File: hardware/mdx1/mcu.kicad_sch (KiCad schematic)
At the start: 37 parts, among them J5 SWD 10p 1.27mm, J6 microSD (Hirose DM3AT), U22 STM32H743ZIT6, Y1 16.384 MHz 3225, Y2 32.768 kHz 3215

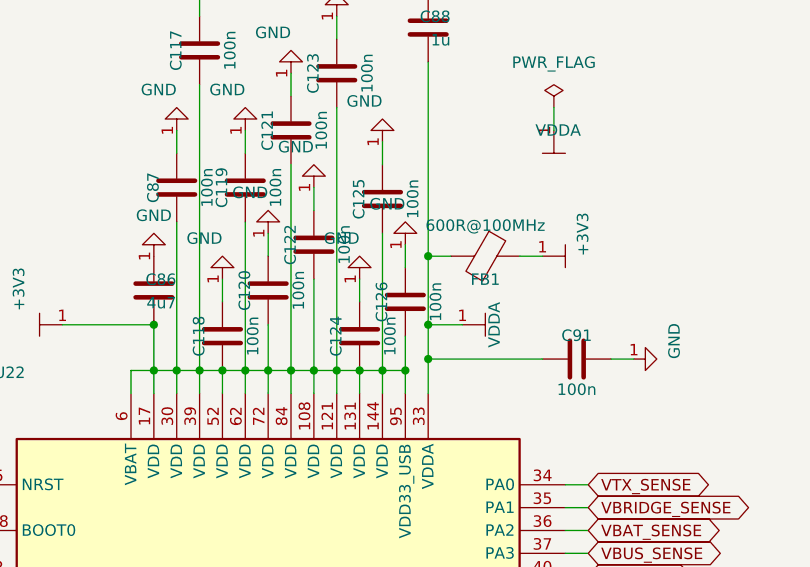
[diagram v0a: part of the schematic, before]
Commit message: Re-source out-of-stock parts; rework D8/9 footprint and GNSS antenna front end
Parts re-sourced to in-stock equivalents (BOM + board + firmware kept in sync):
- U4  TPS65131RGET, U12 INA241A2QDGKRQ1, U23 LSM6DSO32TR (same footprints)
- Q1  SiR680ADP-T1-UE3 (80 V, same PowerPAK SO-8; higher Qg - verify gate drive)
- U2  BQ27441DRZT-G1A (drop-in, R9 sense retained)
- D8/9 NSVBAT54SWT1G: SOT-323/SC-70 dual-series wired as a single diode
  (anode=pin1, cathode=pin3, pin2 NC); footprint changed on the board
- C32/C33/C38-48 re-sourced (KEMET/Murata/TDK), same footprints

GNSS antenna: chip antenna -> external active antenna via u.FL
- Removed U28 (chip antenna), C115 (match pad), R111 (0R RF series-match)
- Added J13 u.FL (Molex 73412-0110) + bias-tee: L8 27nH feed, C127 33pF DC block,
  C128 10nF VCC_RF bypass, D17 PESD0402-140 ESD (verify Vrwm >= 5 V)

Firmware:
- mdx_config.h: MDX_ITX_V_PER_A 0.4 -> 1.0 (INA241A2 is 50 V/V, not 20)
- hal_stm32.c: LSM6DSO32 accel init 0x48 -> 0x40 (FS_XL encoding differs; keeps +-4 g)
- make test: 96 checks pass

BOM: bom_data.json reconciled to the updated board (every placed part has an MPN;
fab BOM drops only the 15 test points). Regenerated JLCPCB fab package and the
DigiKey upload BOM (grouped by MPN, compact references).
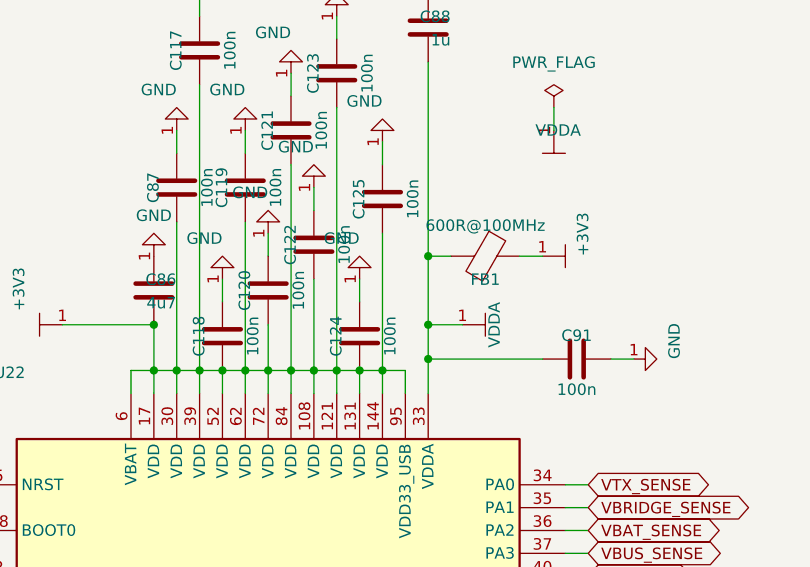
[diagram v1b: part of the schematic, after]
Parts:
- removed C126: 100n, Capacitor_SMD:C_0402_1005Metric, symbol Device:C
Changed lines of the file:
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@@
 	)
 	(junction
-		(at 314.96 153.67)
-		(diameter 0)
-		(color 0 0 0 0)
-	)
-	(junction
 		(at 307.34 153.67)
 		(diameter 0)
@@
 	(wire
 		(pts
-			(xy 314.96 149.86) (xy 314.96 153.67)
-		)
-		(stroke
-			(width 0)
-			(type default)
-		)
-	)
-	(wire
-		(pts
 			(xy 443.23 307.34) (xy 440.69 307.34)
 		)
@@
 	(wire
 		(pts
-			(xy 314.96 142.24) (xy 314.96 139.7)
-		)
-		(stroke
-			(width 0)
-			(type default)
-		)
-	)
-	(wire
-		(pts
 			(xy 332.74 196.85) (xy 335.28 196.85)
 		)
@@
 	)
 	(symbol
-		(lib_id "Device:C")
-		(at 314.96 146.05 180)
-		(unit 1)
-		(body_style 1)
-		(exclude_from_sim no)
-		(in_bom yes)
-		(on_board yes)
-		(in_pos_files yes)
-		(dnp no)
-		(property "Reference" "C126"
-			(at 312.36 146.05 90)
-			(show_name no)
-			(do_not_autoplace no)
-			(effects
-				(font
-					(size 1.27 1.27)
-				)
-			)
-		)
-		(property "Value" "100n"
-			(at 318.36 146.05 90)
-			(show_name no)
-			(do_not_autoplace no)
-			(effects
-				(font
-					(size 1.27 1.27)
-				)
-			)
-		)
-		(property "Footprint" "Capacitor_SMD:C_0402_1005Metric"
-			(at 314.96 146.05 0)
-			(hide yes)
-			(show_name no)
-			(do_not_autoplace no)
-			(effects
-				(font
-					(size 1.27 1.27)
-				)
-			)
-		)
-		(property "Datasheet" ""
-			(at 314.96 146.05 0)
-			(hide yes)
-			(show_name no)
-			(do_not_autoplace no)
-			(effects
-				(font
-					(size 1.27 1.27)
-				)
-			)
-		)
-		(property "Description" ""
-			(at 314.96 146.05 0)
-			(show_name no)
-			(do_not_autoplace no)
-			(effects
-				(font
-					(size 1.27 1.27)
-				)
-			)
-		)
-		(property "Attach" "U22:17"
-			(at 314.96 146.05 0)
-			(hide yes)
-			(show_name no)
-			(do_not_autoplace no)
-			(effects
-				(font
-					(size 1.27 1.27)
-				)
-			)
-		)
-		(pin "1"
-		)
-		(pin "2"
-		)
-		(instances
-			(project "mdx1"
-				(path "/0afcd34a-d204-4875-aae8-4ddd790eda23/7129f8c9-b0b9-4102-87e1-4f134a8471f6"
-					(reference "C126")
-					(unit 1)
-				)
-			)
-		)
-	)
-	(symbol
 		(lib_id "MDX_PWR:+3V3")
 		(at 401.32 313.69 270)
@@
 					(unit 1)
 				)
-			)
-		)
-	)
-	(symbol
-		(lib_id "MDX_PWR:GND")
-		(at 314.96 139.7 180)
-		(unit 1)
-		(body_style 1)
-		(exclude_from_sim no)
-		(in_bom no)
-		(on_board no)
-		(in_pos_files yes)
-		(dnp no)
-		(property "Reference" "#PWR0412"
-			(at 314.96 139.7 0)
-			(hide yes)
-			(show_name no)
-			(do_not_autoplace no)
-			(effects
-				(font
-					(size 1.27 1.27)
-				)
-			)
-		)
-		(property "Value" "GND"
-			(at 314.96 135.2 0)
-			(show_name no)
-			(do_not_autoplace no)
-			(effects
-				(font
-					(size 1.27 1.27)
-				)
-				(justify left)
-			)
-		)
-		(property "Footprint" ""
-			(at 314.96 139.7 0)
-			(hide yes)
-			(show_name no)
-			(do_not_autoplace no)
-			(effects
-				(font
-					(size 1.27 1.27)
-				)
-			)
-		)
-		(property "Datasheet" ""
-			(at 314.96 139.7 0)
-			(hide yes)
-			(show_name no)
-			(do_not_autoplace no)
-			(effects
-				(font
-					(size 1.27 1.27)
-				)
-			)
-		)
-		(property "Description" ""
-			(at 314.96 139.7 0)
-			(show_name no)
-			(do_not_autoplace no)
-			(effects
-				(font
-					(size 1.27 1.27)
-				)
-			)
-		)
-		(pin "1"
-		)
-		(instances
-			(project "mdx1"
-				(path "/0afcd34a-d204-4875-aae8-4ddd790eda23/7129f8c9-b0b9-4102-87e1-4f134a8471f6"
-					(reference "#PWR0412")
-					(unit 1)
-				)

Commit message: Add LL-audio + expansion-header support (firmware, schematic nets, mount holes)
Firmware (host bench 96/0):
- Optional low-latency audio module (nRF52840 daughterboard on J14): settings
  item "Low-latency audio" + "Pair LL headphones" (auto-exposed to UI and app via
  the item table), settings_t.ll_audio, HAL hal_ll_audio_*(), USART3 (PD8/PD9) +
  PG0/PG1 on the target; BM83 kept for BLE/app + standard-BT audio. Sim stubs.
- Expansion header: I2C4 (PF14/PF15), SPI2 (PB13/14/15, CS PG8), UART5 (PB6/PB12),
  GPIO PE13/PA15 initialised; portable hal_exp_*() API + sim stubs.

Schematic: J14 LL-audio header and expansion-header nets wired to the MCU; cleared
the no-connect flags on the newly used STM32 pins (PD8/9, PG0/1, PF14/15, PB13/14/15,
PG8, PB6, PB12, PE13, PA15).

Board: added 4x M3 (3.2 mm) mounting holes (H1-H4) to the main board at the
enclosure positions (128 x 85 mm rectangle, 3.55 mm inset).

Docs: firmware guide menu, design report (IMU), staged bring-up, and the priced BOM
review updated for the current part set.
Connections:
- net EXP_GPIO2: now reaches U22.110 (PA15)
- net EXP_UART_TX: now reaches U22.136 (PB6)
- net EXP_I2C_SCL: now reaches U22.54 (PF14)
- net EXP_I2C_SDA: now reaches U22.55 (PF15)
- net NRF_RESET: now reaches U22.56 (PG0)
- net NRF_STATUS: now reaches U22.57 (PG1)
- net EXP_GPIO1: now reaches U22.66 (PE13)
- net EXP_UART_RX: now reaches U22.73 (PB12)
- net EXP_SPI_SCK: now reaches U22.74 (PB13)
- net EXP_SPI_MISO: now reaches U22.75 (PB14)
- net EXP_SPI_MOSI: now reaches U22.76 (PB15)
- net NRF_RXD: now reaches U22.77 (PD8)
- net NRF_TXD: now reaches U22.78 (PD9)
- net EXP_SPI_CS: now reaches U22.93 (PG8)
- no-connect marks 39 -> 25
